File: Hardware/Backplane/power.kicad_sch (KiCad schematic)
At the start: 56 parts, among them J901 Conn_01x05, U101 P2X8C4M64P, U901 AP3445LW6-7

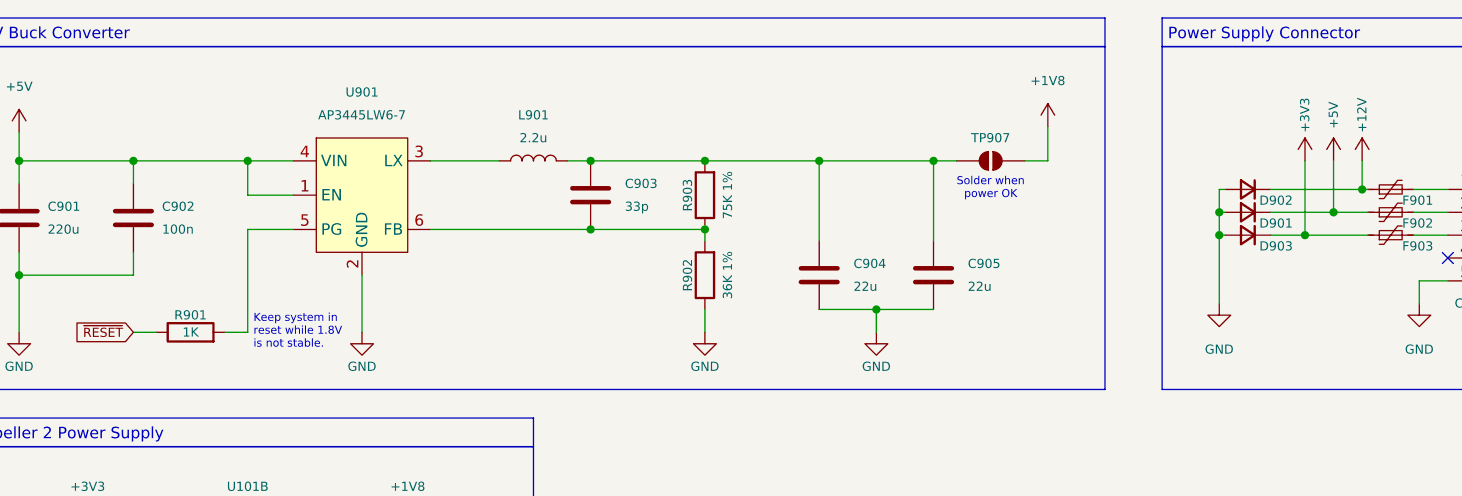
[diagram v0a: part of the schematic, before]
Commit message: Some work on the backplane schematics: Improves module locality
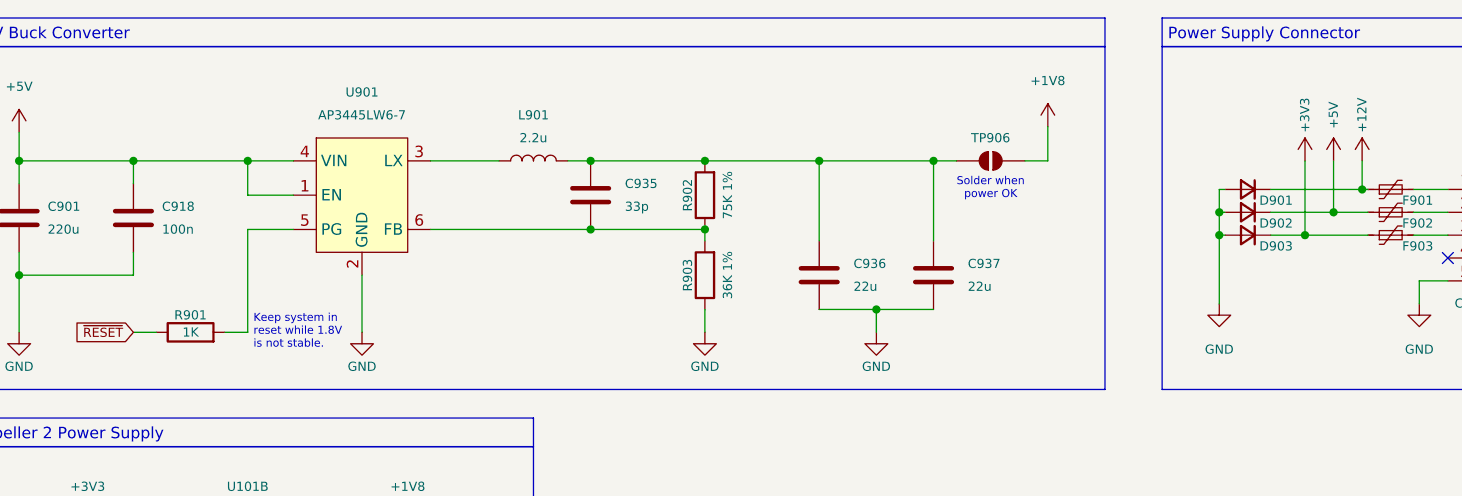
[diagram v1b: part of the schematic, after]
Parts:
- renumbered C906 to C902, C907 to C903, C908 to C904, C909 to C905, C910 to C906, C911 to C907, C912 to C908, C913 to C909, C914 to C910, C915 to C911, C916 to C912, C917 to C913, C918 to C914, C919 to C915, C920 to C916, C921 to C917, C902 to C918, C922 to C919, C923 to C920, C924 to C921, C925 to C922, C926 to C923, C927 to C924, C928 to C925, C929 to C926, C930 to C927, C931 to C928, C932 to C929, C933 to C930, C934 to C931, C935 to C932, C936 to C933, C937 to C934, C903 to C935, C904 to C936, C905 to C937, D902 to D901, D901 to D902, R903 to R902, R902 to R903, TP907 to TP906

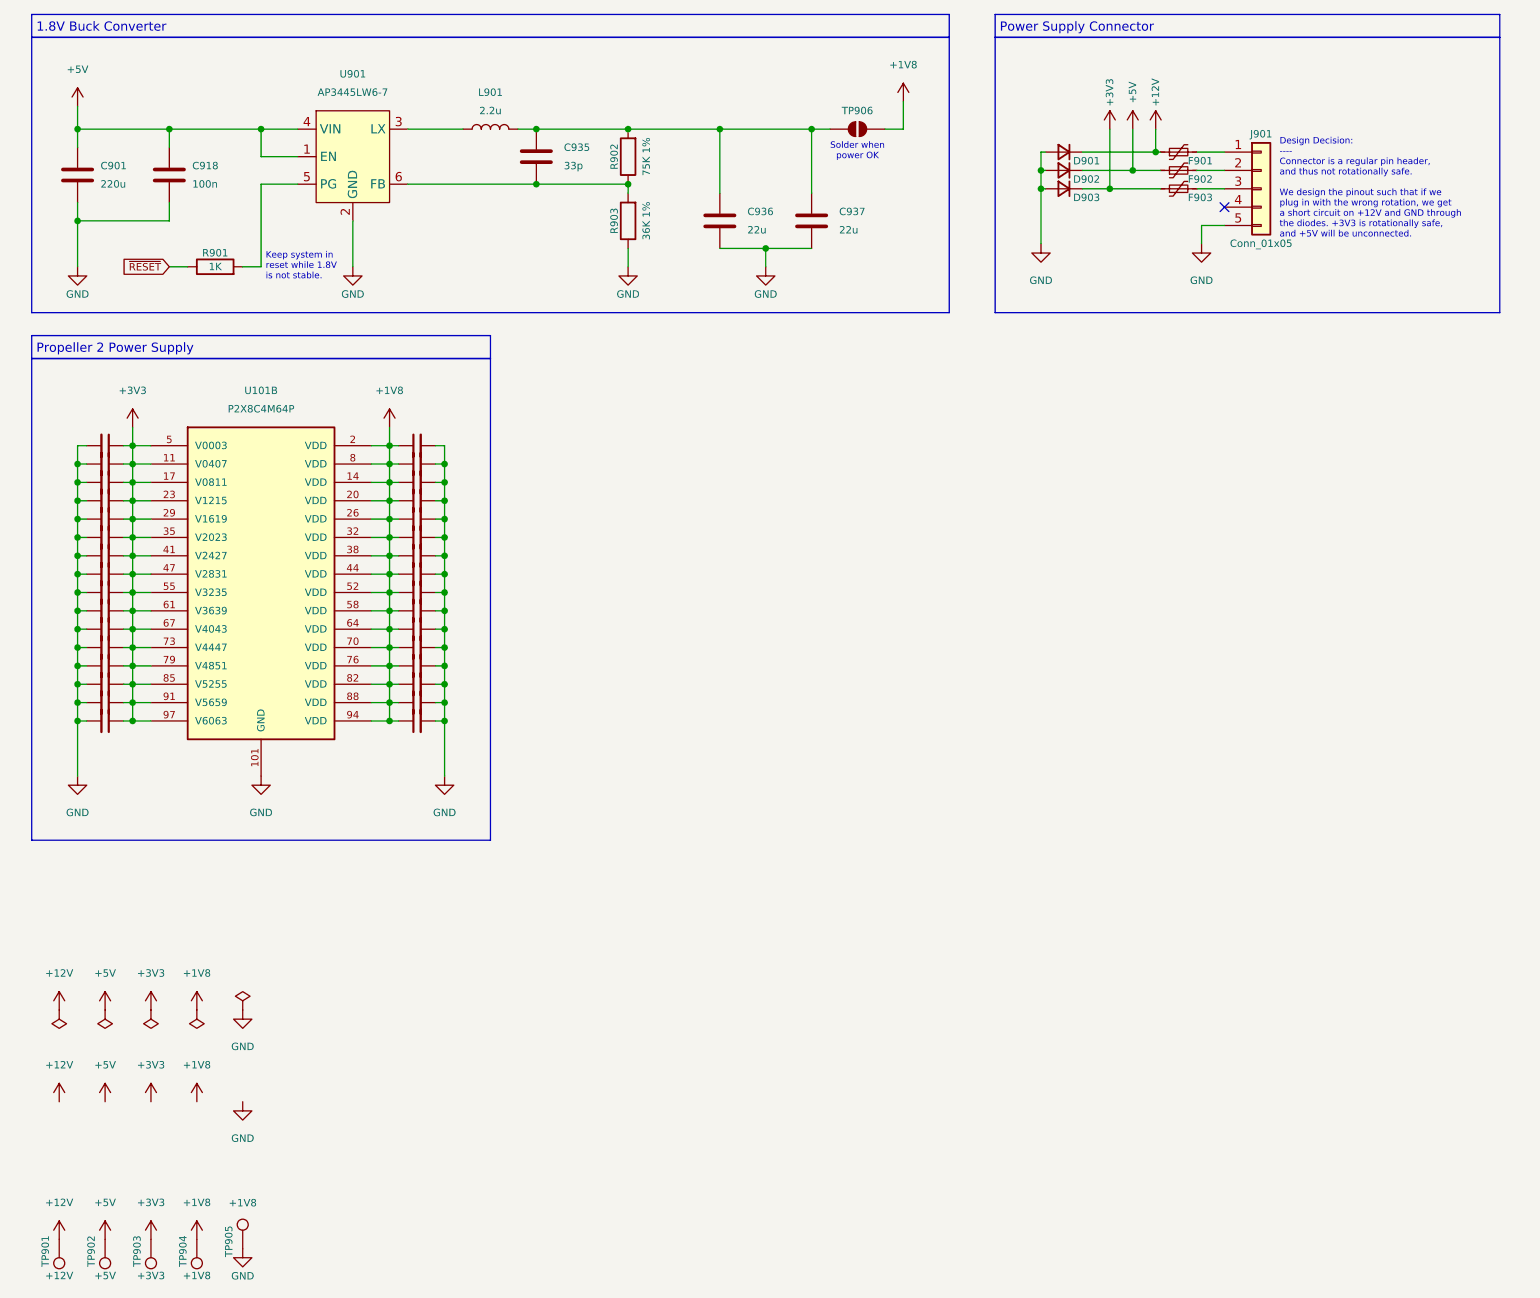
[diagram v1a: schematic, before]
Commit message: Starts to implement a tool to generate symbols for KiCAD from a generic description.
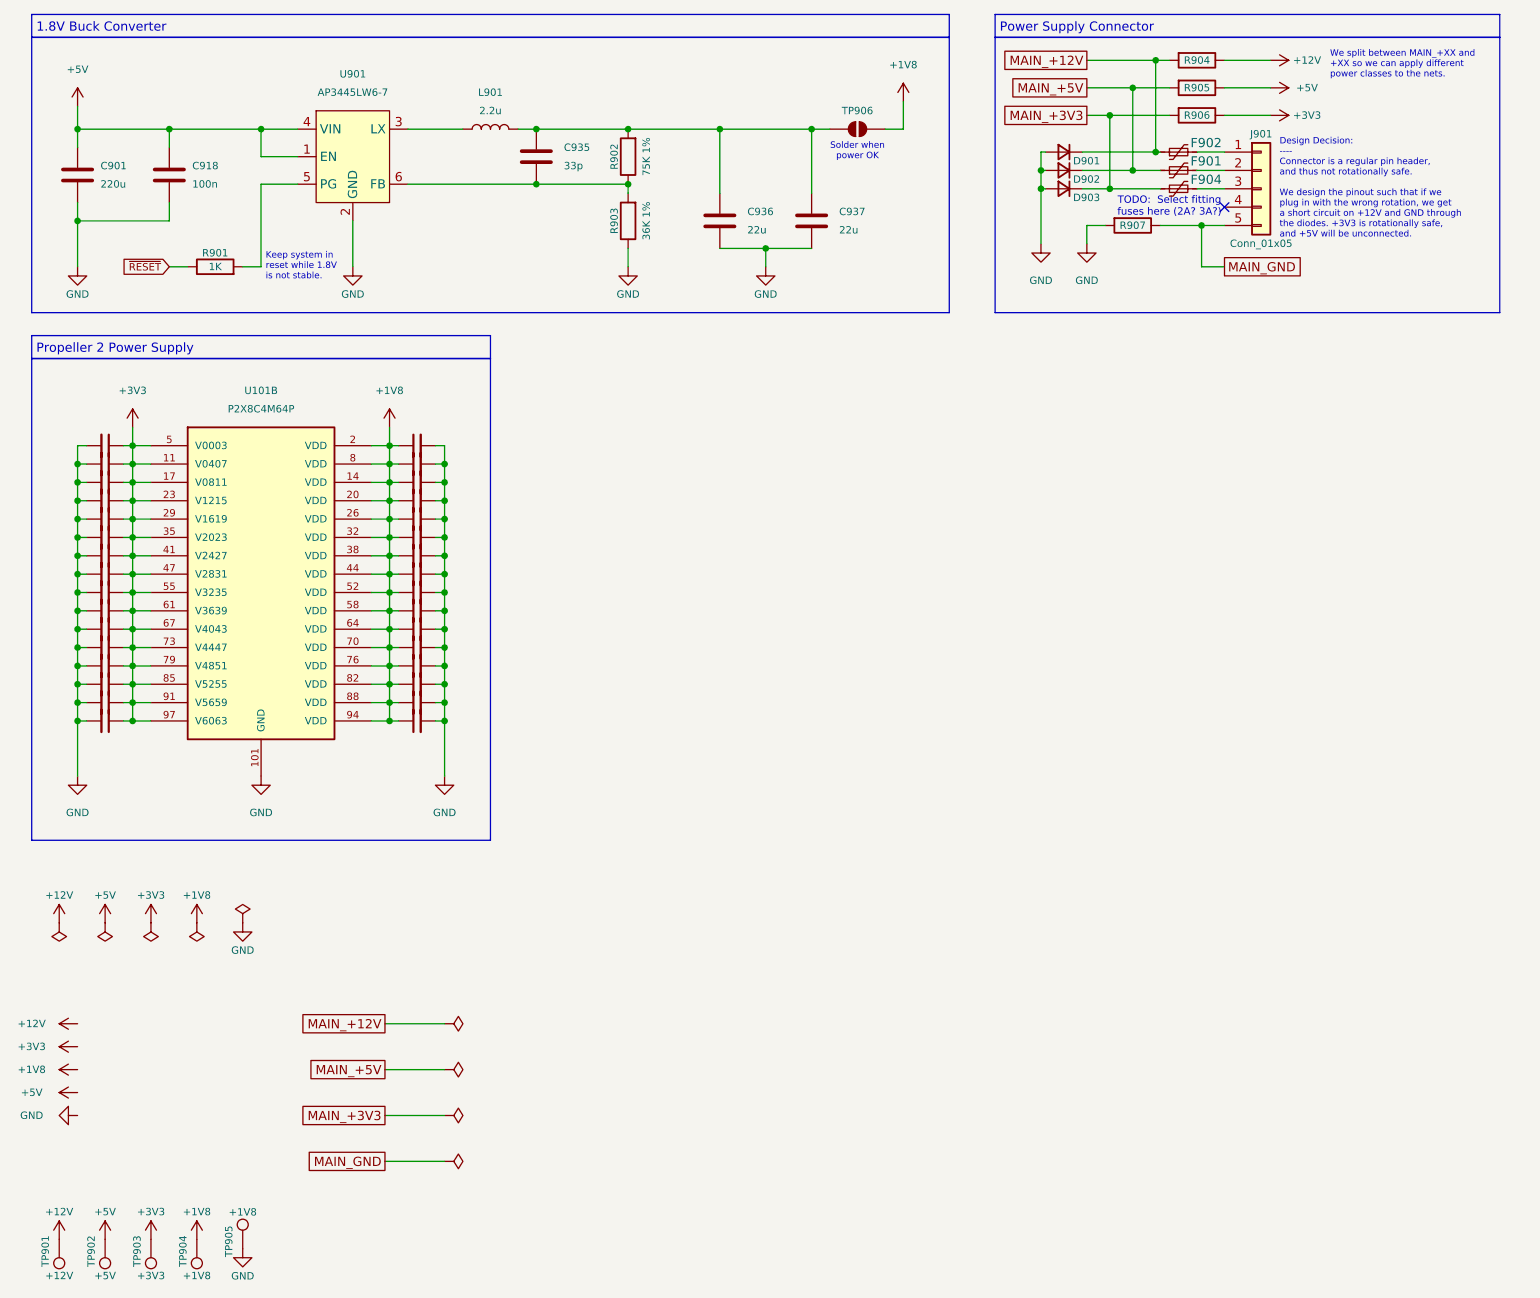
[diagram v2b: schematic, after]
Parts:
- removed F901, F902, F903: Polyfuse_Small, Fuse:Fuse_1206_3216Metric, symbol Device:Polyfuse_Small
- added F901, F902, F904: SMD1206B050TF/15, symbol Symbol Library:SMD1206B050TF/15
- added R904, R905, R906, R907: 0, Resistor_SMD:R_0603_1608Metric, symbol Device:R
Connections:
- net +12V: now also R904.1; no longer D901.1 (K)
- net +3V3: now also R906.1; no longer D903.1 (K)
- net +5V: now also R905.1; no longer D902.1 (K)
- net GND: now also R907.2; no longer J901.5 (Pin_5)
- net at J901.1 (Pin_1): now also F902.2
- net at J901.3 (Pin_3): now also F904.2
- net at J901.2 (Pin_2): now also F901.2
- new net MAIN_+12V: D901.1 (K), F902.1, R904.2
- new net MAIN_+3V3: D903.1 (K), F904.1, R906.2
- new net MAIN_+5V: D902.1 (K), F901.1, R905.2
- new net MAIN_GND: J901.5 (Pin_5), R907.1
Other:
- note added: "TODO: Select fitting fuses here (2A? 3A?)"
- note added: "We split between MAIN_+XX and +XX so we can apply different power classes to the nets."

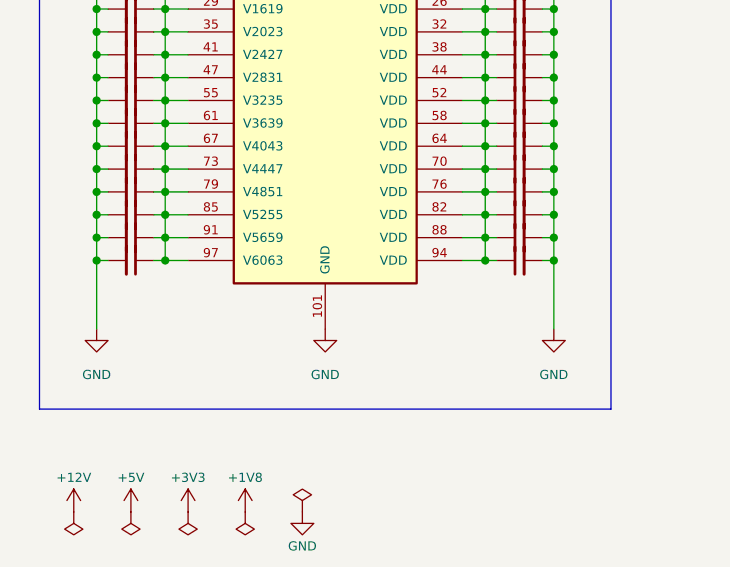
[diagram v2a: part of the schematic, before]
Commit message: Cleans up schematic, adds clean RESET gating
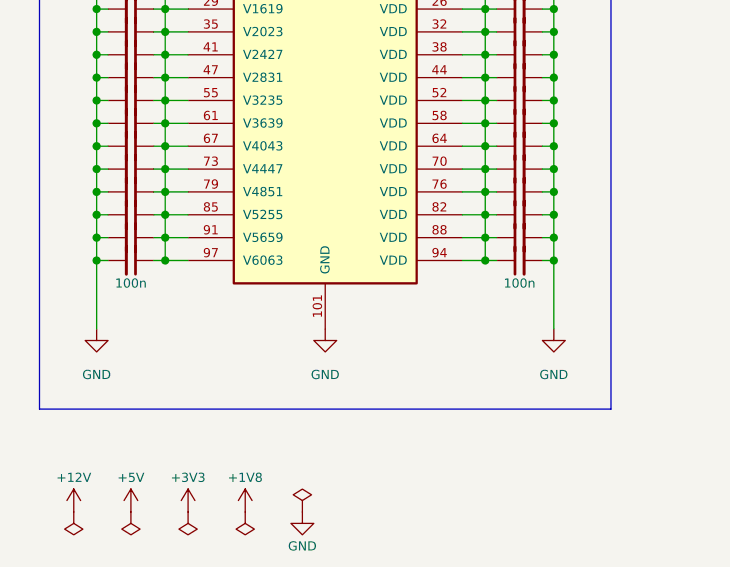
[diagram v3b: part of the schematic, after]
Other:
- company: (none) -> Ashet Technologies
- title: (none) -> Power Management
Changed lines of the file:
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@@
 	(generator_version "9.0")
 	(paper "A4")
+	(title_block
+		(title "Power Management")
+		(company "Ashet Technologies")
+		(comment 1 "This sheet contains all parts related to system-wide power management.")
+	)
 	(rectangle
 		(start 152.4 19.05)
@@
 		(on_board yes)
 		(dnp no)
-		(fields_autoplaced yes)
 		(property "Reference" "C917"
 			(at 29.2037 110.49 90)
@@
 		)
 		(property "Value" "100n"
-			(at 29.2037 113.03 90)
+			(at 29.21 119.38 90)
 			(effects
 				(font
 					(size 1.016 1.016)
 				)
-				(hide yes)
 			)
 		)
@@
 		(on_board yes)
 		(dnp no)
-		(fields_autoplaced yes)
 		(property "Reference" "C934"
 			(at 72.3963 110.49 90)
@@
 		)
 		(property "Value" "100n"
-			(at 72.3963 113.03 90)
+			(at 72.39 119.38 90)
 			(effects
 				(font
 					(size 1.016 1.016)
 				)
-				(hide yes)
 			)
 		)

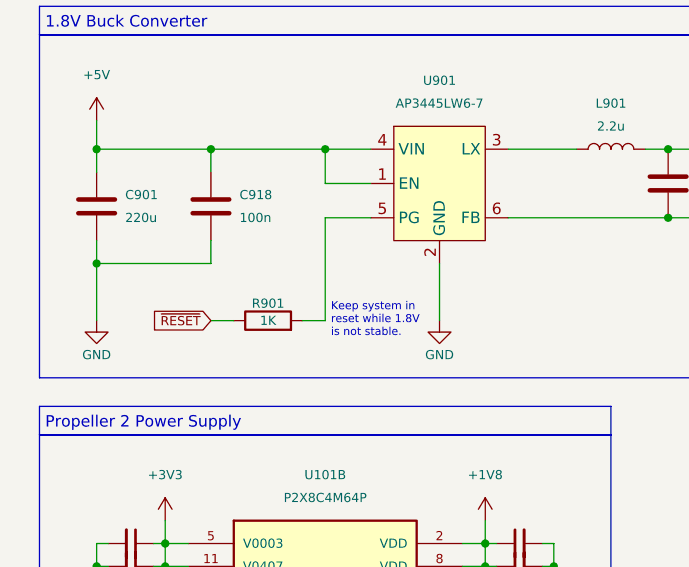
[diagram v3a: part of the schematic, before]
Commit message: Updates backplane: Improves voltage measurement dividers, replaces DS1307+ RTC with a much cheaper one, replaces 8 MHz global clock with 48 MHz global clock
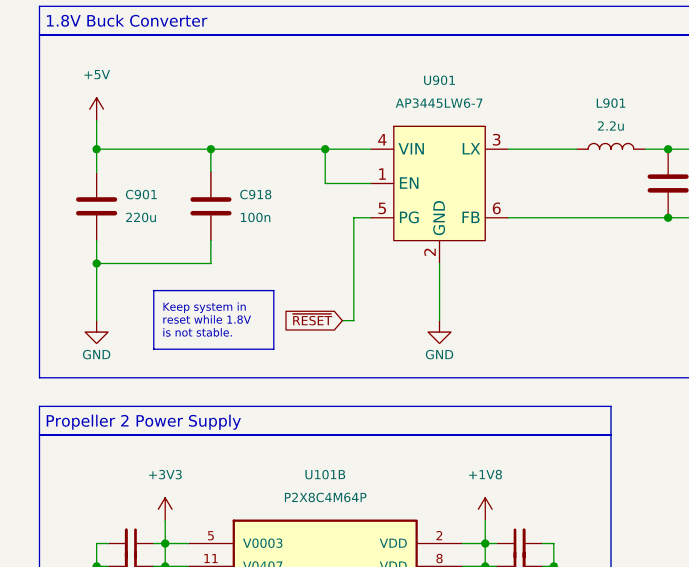
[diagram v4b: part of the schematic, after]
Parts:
- removed R901: 1K, Resistor_SMD:R_0603_1608Metric, symbol Device:R
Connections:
- net ~{RESET}: now also U901.5 (PG)
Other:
- note removed: "Keep system in reset while 1.8V is not stable."
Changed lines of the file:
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@@
 		)
 	)
-	(text "Keep system in\nreset while 1.8V\nis not stable."
+	(text "We split between MAIN_+XX and\n+XX so we can apply different\npower classes to the nets."
 		(exclude_from_sim no)
-		(at 51.435 53.975 0)
+		(at 198.755 26.035 0)
 		(effects
 			(font
@@
 		)
 	)
-	(text "We split between MAIN_+XX and\n+XX so we can apply different\npower classes to the nets."
+	(text "Design Decision:\n----\nConnector is a regular pin header,\nand thus not rotationally safe.\n\nWe design the pinout such that if we\nplug in with the wrong rotation, we get\na short circuit on +12V and GND through\nthe diodes. +3V3 is rotationally safe,\nand +5V will be unconnected."
 		(exclude_from_sim no)
-		(at 198.755 26.035 0)
+		(at 191.77 43.18 0)
 		(effects
 			(font
@@
 		)
 	)
-	(text "Design Decision:\n----\nConnector is a regular pin header,\nand thus not rotationally safe.\n\nWe design the pinout such that if we\nplug in with the wrong rotation, we get\na short circuit on +12V and GND through\nthe diodes. +3V3 is rotationally safe,\nand +5V will be unconnected."
+	(text_box "Keep system in\nreset while 1.8V\nis not stable."
 		(exclude_from_sim no)
-		(at 191.77 43.18 0)
+		(at 31.75 50.6348 0)
+		(size 13.335 6.5152)
+		(margins 0.9525 0.9525 0.9525 0.9525)
+		(stroke
+			(width 0)
+			(type default)
+		)
+		(fill
+			(type color)
+			(color 255 255 255 1)
+		)
 		(effects
 			(font
@@
 	(wire
 		(pts
-			(xy 48.26 53.975) (xy 50.8 53.975)
-		)
-		(stroke
-			(width 0)
-			(type default)
-		)
-	)
-	(wire
-		(pts
 			(xy 74.93 88.9) (xy 76.2 88.9)
 		)
@@
 	(wire
 		(pts
-			(xy 55.88 42.545) (xy 50.8 42.545)
+			(xy 55.88 42.545) (xy 53.975 42.545)
 		)
 		(stroke
@@
 	(wire
 		(pts
-			(xy 50.8 42.545) (xy 50.8 53.975)
+			(xy 53.975 42.545) (xy 53.975 53.975)
 		)
 		(stroke
@@
 	(wire
 		(pts
-			(xy 38.1 53.975) (xy 40.64 53.975)
-		)
-		(stroke
-			(width 0)
-			(type default)
-		)
-	)
-	(wire
-		(pts
 			(xy 74.93 114.3) (xy 76.2 114.3)
 		)
@@
 	(wire
 		(pts
+			(xy 52.705 53.975) (xy 53.975 53.975)
+		)
+		(stroke
+			(width 0)
+			(type default)
+		)
+	)
+	(wire
+		(pts
 			(xy 33.02 114.3) (xy 31.75 114.3)
 		)
@@
 	(global_label "~{RESET}"
 		(shape input)
-		(at 38.1 53.975 180)
+		(at 52.705 53.975 180)
 		(fields_autoplaced yes)
 		(effects
@@
 		)
 		(property "Intersheetrefs" "${INTERSHEET_REFS}"
-			(at 29.3697 53.975 0)
+			(at 43.9747 53.975 0)
 			(effects
 				(font
@@
 					(unit 1)
 				)
-			)
-		)
-	)
-	(symbol
-		(lib_id "Device:R")
-		(at 44.45 53.975 90)
-		(unit 1)
-		(exclude_from_sim no)
-		(in_bom yes)
-		(on_board yes)
-		(dnp no)
-		(property "Reference" "R901"
-			(at 44.45 52.07 90)
-			(effects
-				(font
-					(size 1.016 1.016)
-				)
-			)
-		)
-		(property "Value" "1K"
-			(at 44.45 53.975 90)
-			(effects
-				(font
-					(size 1.016 1.016)
-				)
-			)
-		)
-		(property "Footprint" "Resistor_SMD:R_0603_1608Metric"
-			(at 44.45 55.753 90)
-			(effects
-				(font
-					(size 1.27 1.27)
-				)
-				(hide yes)
-			)
-		)
-		(property "Datasheet" ""
-			(at 44.45 53.975 0)
-			(effects
-				(font
-					(size 1.27 1.27)
-				)
-				(hide yes)
-			)
-		)
-		(property "Description" "Resistor"
-			(at 44.45 53.975 0)
-			(effects
-				(font
-					(size 1.27 1.27)
-				)
-				(hide yes)
-			)
-		)
-		(pin "2"
-		)
-		(pin "1"
-		)
-		(instances
-			(project ""
-				(path "/c6da991a-d3ed-4ac1-8b0d-12cd7ba8539b/a6aaca62-686e-49f0-9767-a5ba81511d00"
-					(reference "R901")
-					(unit 1)
-				)
